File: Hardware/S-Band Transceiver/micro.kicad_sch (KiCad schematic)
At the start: 43 parts, among them J3 AVR-UPDI-6, J4 USB_C_Receptacle_USB2.0_16P, SW1 SW_Push, U2 AVR128DA48x-xPT, U3 ADS1118IDGS, U4 FT231XQ

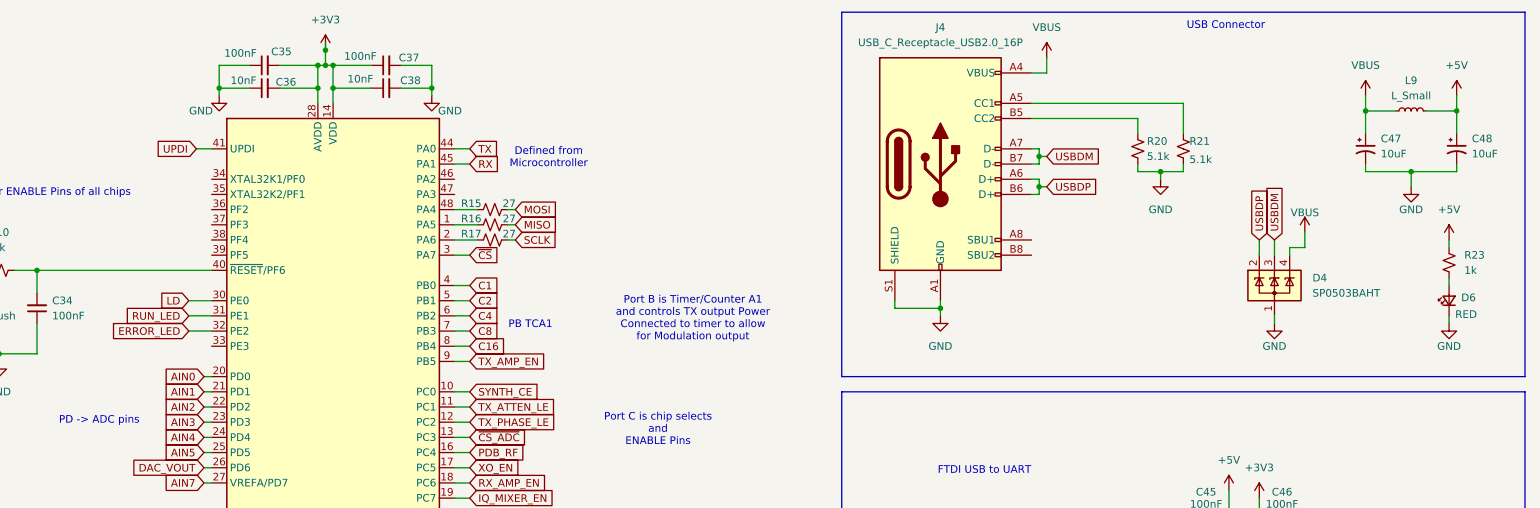
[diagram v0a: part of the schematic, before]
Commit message: Finished assigning footprints and starting board layout
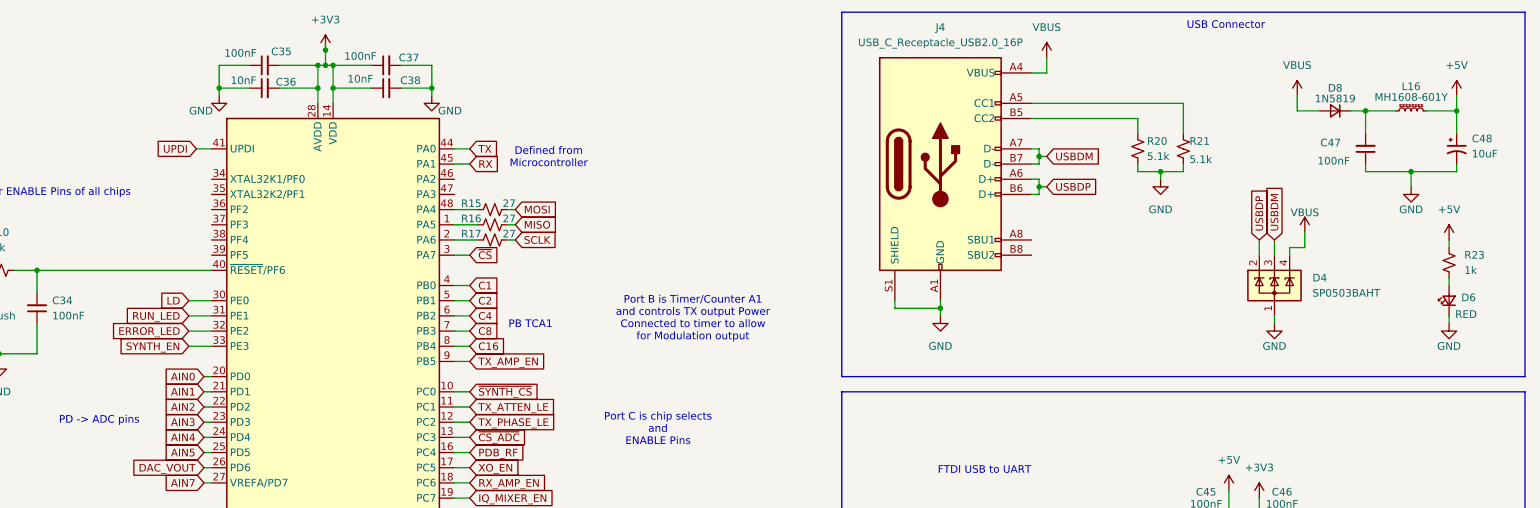
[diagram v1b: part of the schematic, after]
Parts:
- removed C47: 10uF, symbol Device:C_Polarized_Small_US
- removed L9: L_Small, symbol Device:L_Small
- added C47: 100nF, Capacitor_SMD:C_0402_1005Metric, symbol Device:C_Small
- added D8: 1N5819, Diode_SMD:D_SOD-123, symbol Device:D_Small
- added L16: MH1608-601Y, Inductor_SMD:L_0603_1608Metric, symbol Device:L_Ferrite_Small
- C34, C35, C36, C37, C38, C39, C40, C41, C42, C43, C44, C45, C46: footprint (none) -> Capacitor_SMD:C_0402_1005Metric
- C48: footprint (none) -> Capacitor_Tantalum_SMD:CP_EIA-3216-18_Kemet-A
- D2, D3, D5, D6, D7: footprint (none) -> LED_SMD:LED_0805_2012Metric
- J3: footprint (none) -> Connector_IDC:IDC-Header_2x03_P2.54mm_Vertical
- J4: footprint (none) -> Connector_USB:USB_C_Receptacle_GCT_USB4085
- R10, R11, R12, R13, R14, R15, R16, R17, R18, R19, R20, R21, R22, R23, R24: footprint (none) -> Resistor_SMD:R_0603_1608Metric
- SW1: footprint (none) -> Button_Switch_SMD:SW_SPST_B3SL-1002P
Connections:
- net +5V: now also L16.2
- net GND: now also C47.1
- net VBUS: now also D8.2 (A)
- net SYNTH_EN: now reaches U2.33 (PE3)
- net SYNTH_CE renamed ~{SYNTH_CS}
- new net: C47.2, D8.1 (K), L16.1

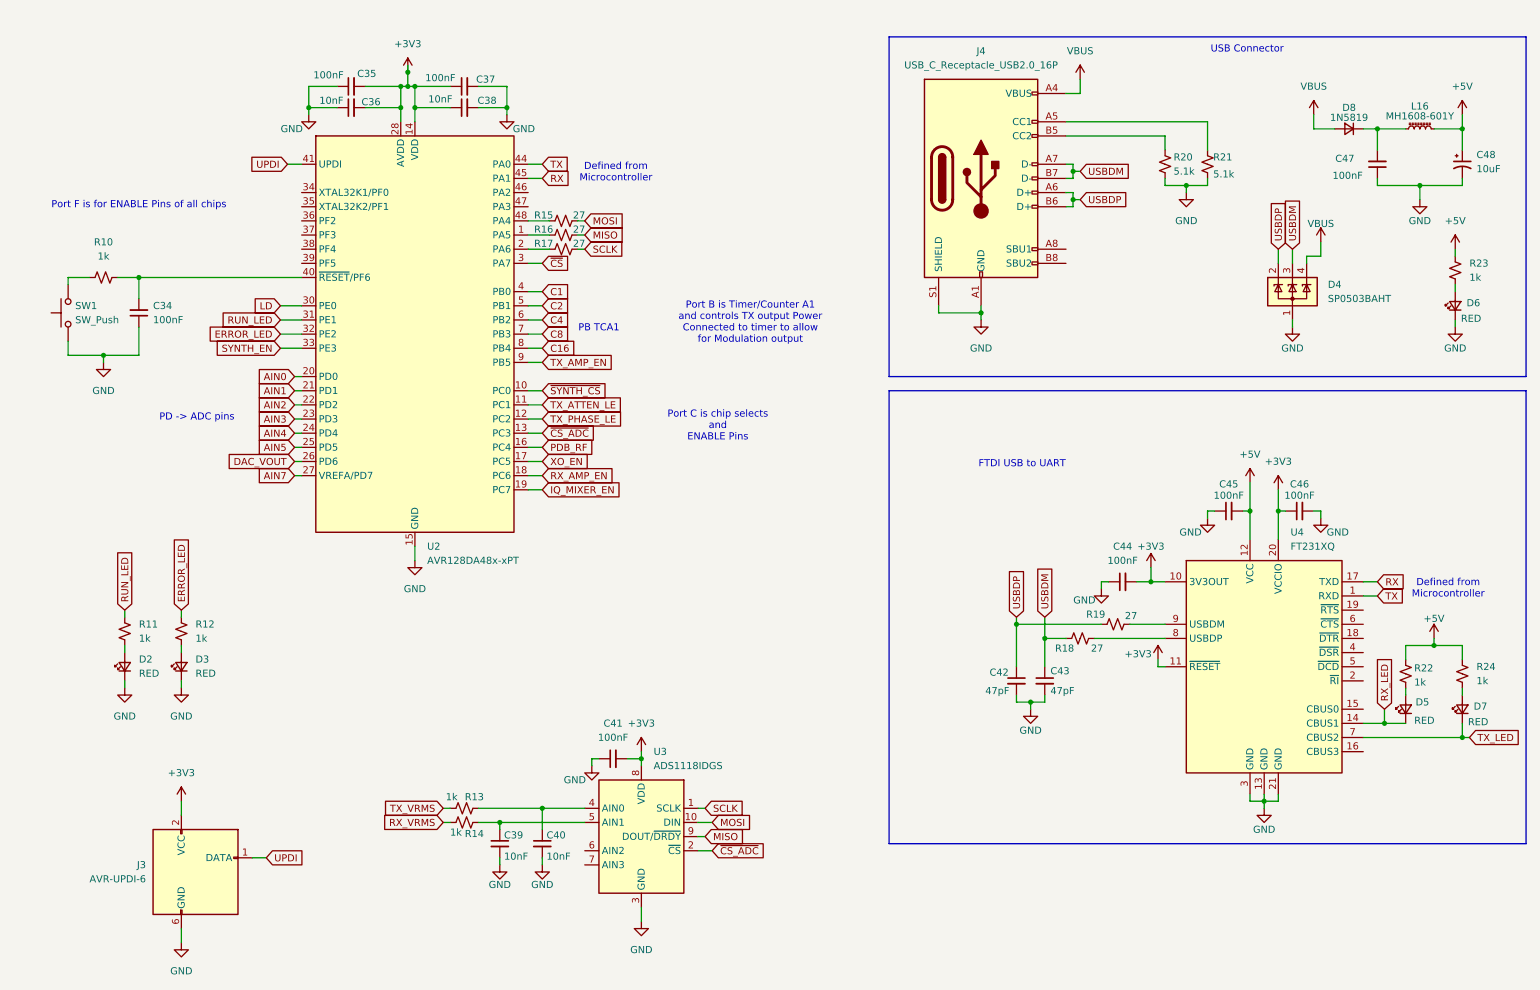
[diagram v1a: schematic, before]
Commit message: Updating Capacitors and LEDs in schematic
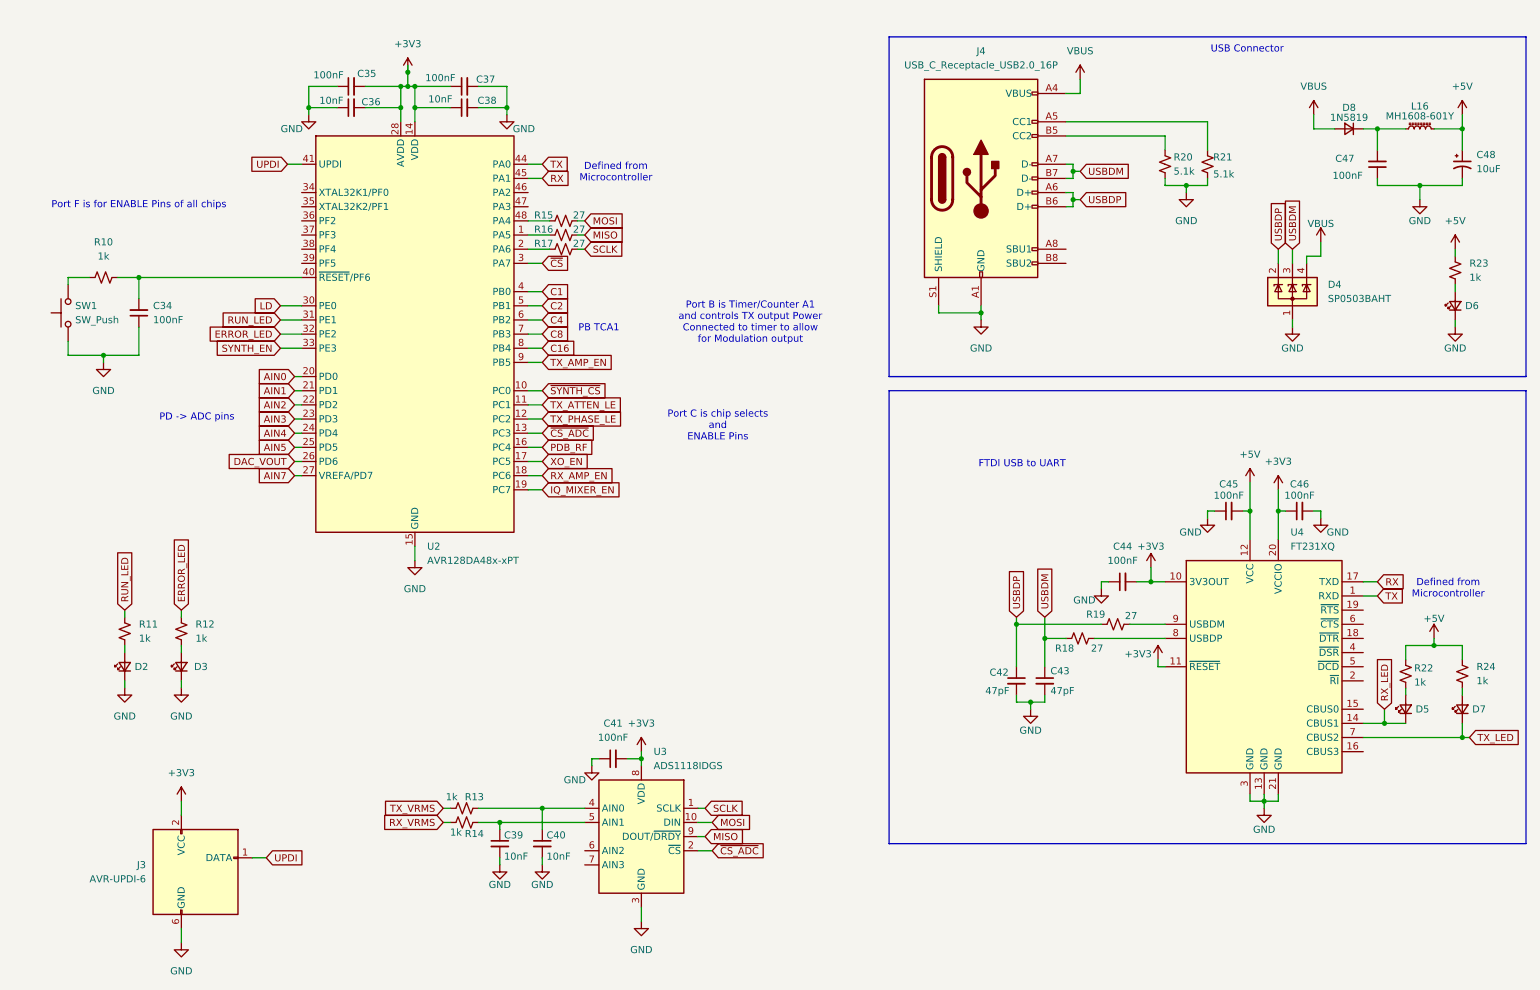
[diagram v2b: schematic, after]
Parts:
- D2, D5, D6, D7: value RED -> 150080VS75000
- D3: value RED -> 150080SS75000

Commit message: Updating board layout and routing
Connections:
- net USBDM: now also C42.1, R19.1; no longer C43.1, R18.1
- net USBDP: now also C43.1, R18.1; no longer C42.1, R19.1

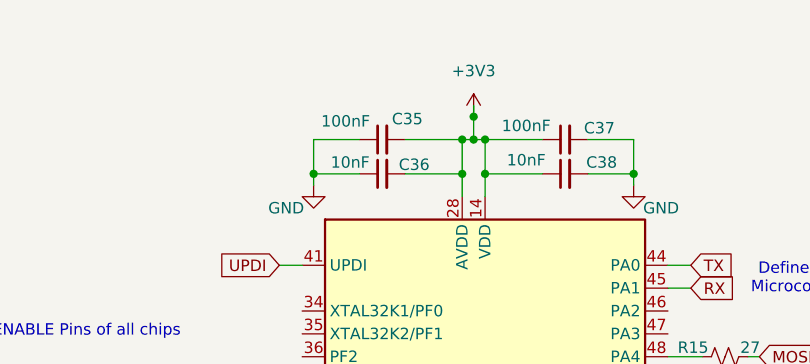
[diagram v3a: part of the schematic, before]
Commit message: Routing microcontroller
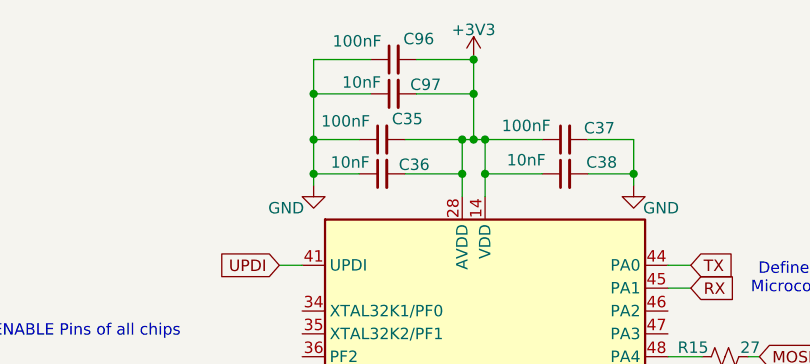
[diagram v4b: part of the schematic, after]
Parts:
- added C96: 100nF, Capacitor_SMD:C_0402_1005Metric, symbol Device:C_Small
- added C97: 10nF, Capacitor_SMD:C_0402_1005Metric, symbol Device:C_Small
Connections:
- net +3V3: now also C96.2, C97.2
- net GND: now also C96.1, C97.1
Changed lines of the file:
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@@
 	)
 	(junction
+		(at 60.96 24.13)
+		(diameter 0)
+		(color 0 0 0 0)
+	)
+	(junction
 		(at 267.97 31.75)
 		(diameter 0)
@@
 	)
 	(junction
-		(at 78.74 21.59)
+		(at 78.74 15.24)
 		(diameter 0)
 		(color 0 0 0 0)
@@
 	)
 	(junction
+		(at 78.74 19.05)
+		(diameter 0)
+		(color 0 0 0 0)
+	)
+	(junction
 		(at 95.25 156.21)
 		(diameter 0)
@@
 	)
 	(junction
+		(at 60.96 19.05)
+		(diameter 0)
+		(color 0 0 0 0)
+	)
+	(junction
 		(at 60.96 27.94)
 		(diameter 0)
@@
 	(wire
 		(pts
+			(xy 72.39 19.05) (xy 78.74 19.05)
+		)
+		(stroke
+			(width 0)
+			(type default)
+		)
+	)
+	(wire
+		(pts
 			(xy 193.04 134.62) (xy 190.5 134.62)
 		)
@@
 	(wire
 		(pts
+			(xy 60.96 15.24) (xy 60.96 19.05)
+		)
+		(stroke
+			(width 0)
+			(type default)
+		)
+	)
+	(wire
+		(pts
 			(xy 27.94 130.81) (xy 27.94 132.08)
 		)
@@
 	(wire
 		(pts
-			(xy 232.41 152.4) (xy 232.41 151.13)
+			(xy 78.74 19.05) (xy 78.74 24.13)
 		)
 		(stroke
@@
 	(wire
 		(pts
-			(xy 254 138.43) (xy 257.81 138.43)
+			(xy 232.41 152.4) (xy 232.41 151.13)
 		)
 		(stroke
@@
 	(wire
 		(pts
-			(xy 91.44 153.67) (xy 102.87 153.67)
+			(xy 254 138.43) (xy 257.81 138.43)
 		)
 		(stroke
@@
 	(wire
 		(pts
-			(xy 252.73 40.64) (xy 252.73 41.91)
+			(xy 91.44 153.67) (xy 102.87 153.67)
 		)
 		(stroke
@@
 	(wire
 		(pts
-			(xy 80.01 106.68) (xy 80.01 109.22)
+			(xy 252.73 40.64) (xy 252.73 41.91)
 		)
 		(stroke
@@
 	(wire
 		(pts
-			(xy 229.87 152.4) (xy 232.41 152.4)
+			(xy 80.01 106.68) (xy 80.01 109.22)
 		)
 		(stroke
@@
 	(wire
 		(pts
-			(xy 78.74 21.59) (xy 78.74 24.13)
+			(xy 229.87 152.4) (xy 232.41 152.4)
 		)
 		(stroke
@@
 	(wire
 		(pts
+			(xy 60.96 19.05) (xy 67.31 19.05)
+		)
+		(stroke
+			(width 0)
+			(type default)
+		)
+	)
+	(wire
+		(pts
 			(xy 213.36 128.27) (xy 213.36 127)
 		)
@@
 	(wire
 		(pts
+			(xy 72.39 15.24) (xy 78.74 15.24)
+		)
+		(stroke
+			(width 0)
+			(type default)
+		)
+	)
+	(wire
+		(pts
 			(xy 252.73 31.75) (xy 257.81 31.75)
 		)
@@
 	(wire
 		(pts
-			(xy 78.74 20.32) (xy 78.74 21.59)
+			(xy 60.96 19.05) (xy 60.96 24.13)
+		)
+		(stroke
+			(width 0)
+			(type default)
+		)
+	)
+	(wire
+		(pts
+			(xy 78.74 15.24) (xy 78.74 19.05)
 		)
 		(stroke
@@
 		)
 	)
+	(wire
+		(pts
+			(xy 60.96 15.24) (xy 67.31 15.24)
+		)
+		(stroke
+			(width 0)
+			(type default)
+		)
+	)
 	(rectangle
 		(start 165.1 78.74)
@@
 	(symbol
 		(lib_id "power:+3V3")
-		(at 78.74 21.59 0)
+		(at 78.74 15.24 0)
 		(unit 1)
 		(exclude_from_sim no)
@@
 		(on_board yes)
 		(dnp no)
-		(fields_autoplaced yes)
 		(property "Reference" "#PWR037"
-			(at 78.74 25.4 0)
+			(at 78.74 19.05 0)
 			(effects
 				(font
@@
 		)
 		(property "Value" "+3V3"
-			(at 78.74 16.51 0)
+			(at 78.74 11.938 0)
 			(effects
 				(font
@@
 		)
 		(property "Footprint" ""
-			(at 78.74 21.59 0)
+			(at 78.74 15.24 0)
 			(effects
 				(font
@@
 		)
 		(property "Datasheet" ""
-			(at 78.74 21.59 0)
+			(at 78.74 15.24 0)
 			(effects
 				(font
@@
 		)
 		(property "Description" "Power symbol creates a global label with name \"+3V3\""
-			(at 78.74 21.59 0)
+			(at 78.74 15.24 0)
 			(effects
 				(font
@@
 	(symbol
 		(lib_id "Device:C_Small")
+		(at 69.85 15.24 90)
+		(unit 1)
+		(exclude_from_sim no)
+		(in_bom yes)
+		(on_board yes)
+		(dnp no)
+		(property "Reference" "C96"
+			(at 72.644 12.954 90)
+			(effects
+				(font
+					(size 1.27 1.27)
+				)
+			)
+		)
+		(property "Value" "100nF"
+			(at 65.786 13.208 90)
+			(effects
+				(font
+					(size 1.27 1.27)
+				)
+			)
+		)
+		(property "Footprint" "Capacitor_SMD:C_0402_1005Metric"
+			(at 69.85 15.24 0)
+			(effects
+				(font
+					(size 1.27 1.27)
+				)
+				(hide yes)
+			)
+		)
+		(property "Datasheet" "~"
+			(at 69.85 15.24 0)
+			(effects
+				(font
+					(size 1.27 1.27)
+				)
+				(hide yes)
+			)
+		)
+		(property "Description" "Unpolarized capacitor, small symbol"
+			(at 69.85 15.24 0)
+			(effects
+				(font
+					(size 1.27 1.27)
+				)
+				(hide yes)
+			)
+		)
+		(pin "2"
+		)
+		(pin "1"
+		)
+		(instances
+			(project "S-Band Transceiver"
+				(path "/811f57cf-e3df-4fba-aff9-353adc85299e/03e3241c-59a9-4f6f-b7cc-ae3fa2c59abc"
+					(reference "C96")
+					(unit 1)
+				)
+			)
+		)
+	)
+	(symbol
+		(lib_id "Device:C_Small")
 		(at 68.58 24.13 90)
 		(unit 1)
@@
 					(unit 1)
 				)
+			)
+		)
+	)
+	(symbol
+		(lib_id "Device:C_Small")
+		(at 69.85 19.05 90)
+		(unit 1)
+		(exclude_from_sim no)
+		(in_bom yes)
+		(on_board yes)
+		(dnp no)
+		(property "Reference" "C97"
+			(at 73.406 18.034 90)
+			(effects
+				(font
+					(size 1.27 1.27)
+				)
+			)
+		)
+		(property "Value" "10nF"
+			(at 66.294 17.78 90)
+			(effects
+				(font
+					(size 1.27 1.27)
+				)
+			)
+		)
+		(property "Footprint" "Capacitor_SMD:C_0402_1005Metric"
+			(at 69.85 19.05 0)
+			(effects
+				(font
+					(size 1.27 1.27)
+				)
+				(hide yes)
+			)
+		)
+		(property "Datasheet" "~"
+			(at 69.85 19.05 0)
+			(effects
+				(font
+					(size 1.27 1.27)
+				)
+				(hide yes)
+			)
+		)
+		(property "Description" "Unpolarized capacitor, small symbol"
+			(at 69.85 19.05 0)
+			(effects
+				(font
+					(size 1.27 1.27)
+				)
+				(hide yes)
+			)
+		)
+		(pin "2"
+		)
+		(pin "1"
+		)
+		(instances
+			(project "S-Band Transceiver"
+				(path "/811f57cf-e3df-4fba-aff9-353adc85299e/03e3241c-59a9-4f6f-b7cc-ae3fa2c59abc"
+					(reference "C97")
+					(unit 1)
+				)

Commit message: Updating routing
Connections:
- net +3V3: no longer C41.2, U3.8 (VDD)
- net RX_AMP_EN: now also U2.17 (PC5); no longer U2.18 (PC6)
- net XO_EN: now also U2.18 (PC6); no longer U2.17 (PC5)
- net IQ_MIXER_EN: no longer names the net of U2.19 (PC7)
- net PDB_RF: no longer names the net of U2.16 (PC4)
- net SYNTH_EN: no longer names the net of U2.33 (PE3)
- new net +3.3VA: C41.2, U3.8 (VDD)
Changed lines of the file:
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@@
 	(wire
 		(pts
-			(xy 100.33 96.52) (xy 102.87 96.52)
-		)
-		(stroke
-			(width 0)
-			(type default)
-		)
-	)
-	(wire
-		(pts
 			(xy 245.11 31.75) (xy 241.3 31.75)
 		)
@@
 	(wire
 		(pts
-			(xy 100.33 88.9) (xy 102.87 88.9)
-		)
-		(stroke
-			(width 0)
-			(type default)
-		)
-	)
-	(wire
-		(pts
 			(xy 187.96 120.65) (xy 203.2 120.65)
 		)
@@
 	(wire
 		(pts
-			(xy 55.88 71.12) (xy 59.69 71.12)
-		)
-		(stroke
-			(width 0)
-			(type default)
-		)
-	)
-	(wire
-		(pts
 			(xy 118.11 144.78) (xy 120.65 144.78)
 		)
@@
 		)
 	)
-	(global_label "PDB_RF"
-		(shape input)
-		(at 102.87 88.9 0)
-		(fields_autoplaced yes)
-		(effects
-			(font
-				(size 1.27 1.27)
-			)
-			(justify left)
-		)
-		(property "Intersheetrefs" "${INTERSHEET_REFS}"
-			(at 112.9914 88.9 0)
-			(effects
-				(font
-					(size 1.27 1.27)
-				)
-				(justify left)
-				(hide yes)
-			)
-		)
-	)
 	(global_label "AIN1"
 		(shape input)
@@
 		)
 	)
-	(global_label "SYNTH_EN"
-		(shape input)
-		(at 55.88 71.12 180)
-		(fields_autoplaced yes)
-		(effects
-			(font
-				(size 1.27 1.27)
-			)
-			(justify right)
-		)
-		(property "Intersheetrefs" "${INTERSHEET_REFS}"
-			(at 43.521 71.12 0)
-			(effects
-				(font
-					(size 1.27 1.27)
-				)
-				(justify right)
-				(hide yes)
-			)
-		)
-	)
 	(global_label "C8"
 		(shape input)
@@
 	(global_label "XO_EN"
 		(shape input)
-		(at 102.87 91.44 0)
+		(at 102.87 93.98 0)
 		(fields_autoplaced yes)
 		(effects
@@
 		)
 		(property "Intersheetrefs" "${INTERSHEET_REFS}"
-			(at 111.8423 91.44 0)
+			(at 111.8423 93.98 0)
 			(effects
 				(font
@@
 	(global_label "RX_AMP_EN"
 		(shape input)
-		(at 102.87 93.98 0)
+		(at 102.87 91.44 0)
 		(fields_autoplaced yes)
 		(effects
@@
 		)
 		(property "Intersheetrefs" "${INTERSHEET_REFS}"
-			(at 116.5594 93.98 0)
+			(at 116.5594 91.44 0)
 			(effects
 				(font
@@
 		)
 	)
-	(global_label "IQ_MIXER_EN"
-		(shape input)
-		(at 102.87 96.52 0)
-		(fields_autoplaced yes)
-		(effects
-			(font
-				(size 1.27 1.27)
-			)
-			(justify left)
-		)
-		(property "Intersheetrefs" "${INTERSHEET_REFS}"
-			(at 117.8899 96.52 0)
-			(effects
-				(font
-					(size 1.27 1.27)
-				)
-				(justify left)
-				(hide yes)
-			)
-		)
-	)
 	(global_label "DAC_VOUT"
 		(shape input)
@@
 	)
 	(symbol
+		(lib_id "power:+3.3VA")
+		(at 120.65 143.51 0)
+		(unit 1)
+		(exclude_from_sim no)
+		(in_bom yes)
+		(on_board yes)
+		(dnp no)
+		(fields_autoplaced yes)
+		(property "Reference" "#PWR043"
+			(at 120.65 147.32 0)
+			(effects
+				(font
+					(size 1.27 1.27)
+				)
+				(hide yes)
+			)
+		)
+		(property "Value" "+3.3VA"
+			(at 120.65 138.43 0)
+			(effects
+				(font
+					(size 1.27 1.27)
+				)
+			)
+		)
+		(property "Footprint" ""
+			(at 120.65 143.51 0)
+			(effects
+				(font
+					(size 1.27 1.27)
+				)
+				(hide yes)
+			)
+		)
+		(property "Datasheet" ""
+			(at 120.65 143.51 0)
+			(effects
+				(font
+					(size 1.27 1.27)
+				)
+				(hide yes)
+			)
+		)
+		(property "Description" "Power symbol creates a global label with name \"+3.3VA\""
+			(at 120.65 143.51 0)
+			(effects
+				(font
+					(size 1.27 1.27)
+				)
+				(hide yes)
+			)
+		)
+		(pin "1"
+		)
+		(instances
+			(project "S-Band Transceiver"
+				(path "/811f57cf-e3df-4fba-aff9-353adc85299e/03e3241c-59a9-4f6f-b7cc-ae3fa2c59abc"
+					(reference "#PWR043")
+					(unit 1)
+				)
+			)
+		)
+	)
+	(symbol
 		(lib_id "Device:R_Small_US")
 		(at 88.9 153.67 90)
@@
 					(unit 1)
 				)
-			)
-		)
-	)
-	(symbol
-		(lib_id "power:+3V3")
-		(at 120.65 143.51 0)
-		(unit 1)
-		(exclude_from_sim no)
-		(in_bom yes)
-		(on_board yes)
-		(dnp no)
-		(fields_autoplaced yes)
-		(property "Reference" "#PWR043"
-			(at 120.65 147.32 0)
-			(effects
-				(font
-					(size 1.27 1.27)
-				)
-				(hide yes)
-			)
-		)
-		(property "Value" "+3V3"
-			(at 120.65 138.43 0)
-			(effects
-				(font
-					(size 1.27 1.27)
-				)
-			)
-		)
-		(property "Footprint" ""
-			(at 120.65 143.51 0)
-			(effects
-				(font
-					(size 1.27 1.27)
-				)
-				(hide yes)
-			)
-		)
-		(property "Datasheet" ""
-			(at 120.65 143.51 0)
-			(effects
-				(font
-					(size 1.27 1.27)
-				)
-				(hide yes)
-			)
-		)
-		(property "Description" "Power symbol creates a global label with name \"+3V3\""
-			(at 120.65 143.51 0)
-			(effects
-				(font
-					(size 1.27 1.27)
-				)
-				(hide yes)
-			)
-		)
-		(pin "1"
-		)
-		(instances
-			(project "S-Band Transceiver"
-				(path "/811f57cf-e3df-4fba-aff9-353adc85299e/03e3241c-59a9-4f6f-b7cc-ae3fa2c59abc"
-					(reference "#PWR043")
-					(unit 1)
-				)
